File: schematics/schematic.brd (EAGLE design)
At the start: 134.6 x 64.8 mm, 25 parts, among them U1 TSR_1-2450

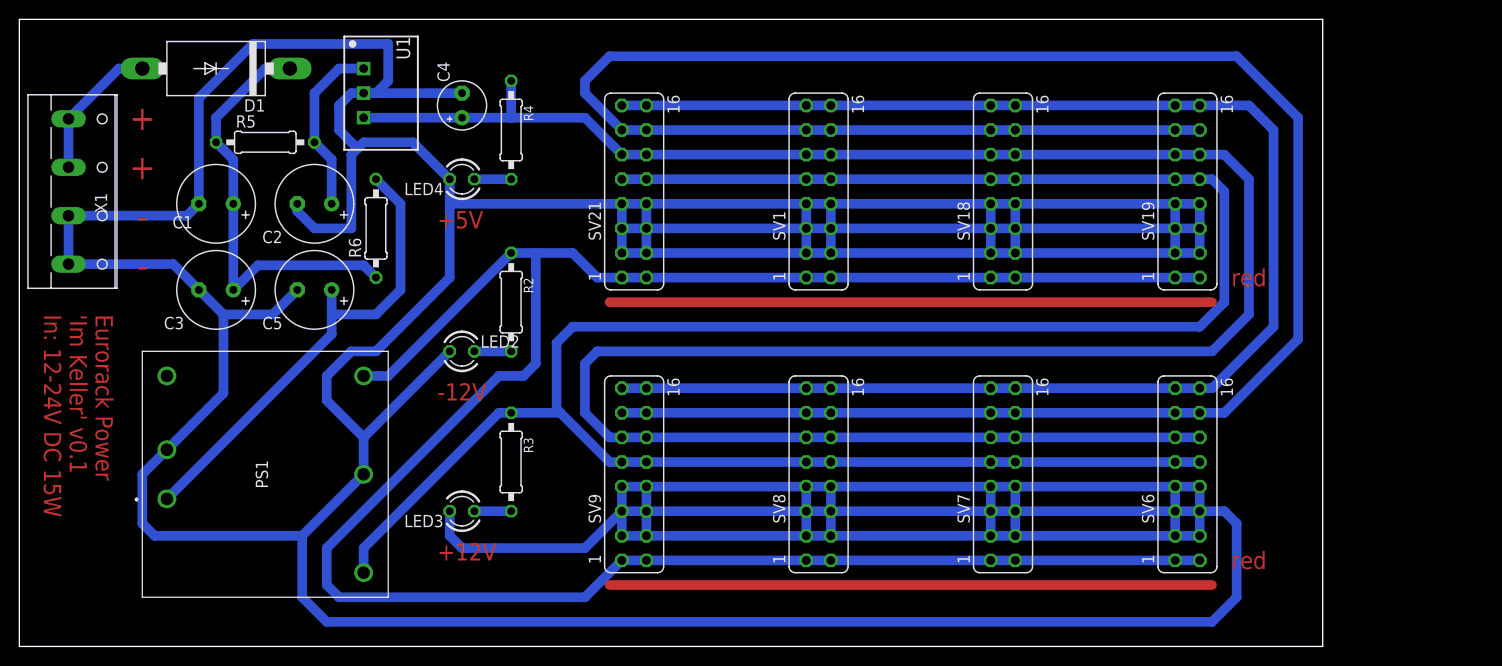
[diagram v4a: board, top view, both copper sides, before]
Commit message: changed distance of power headers
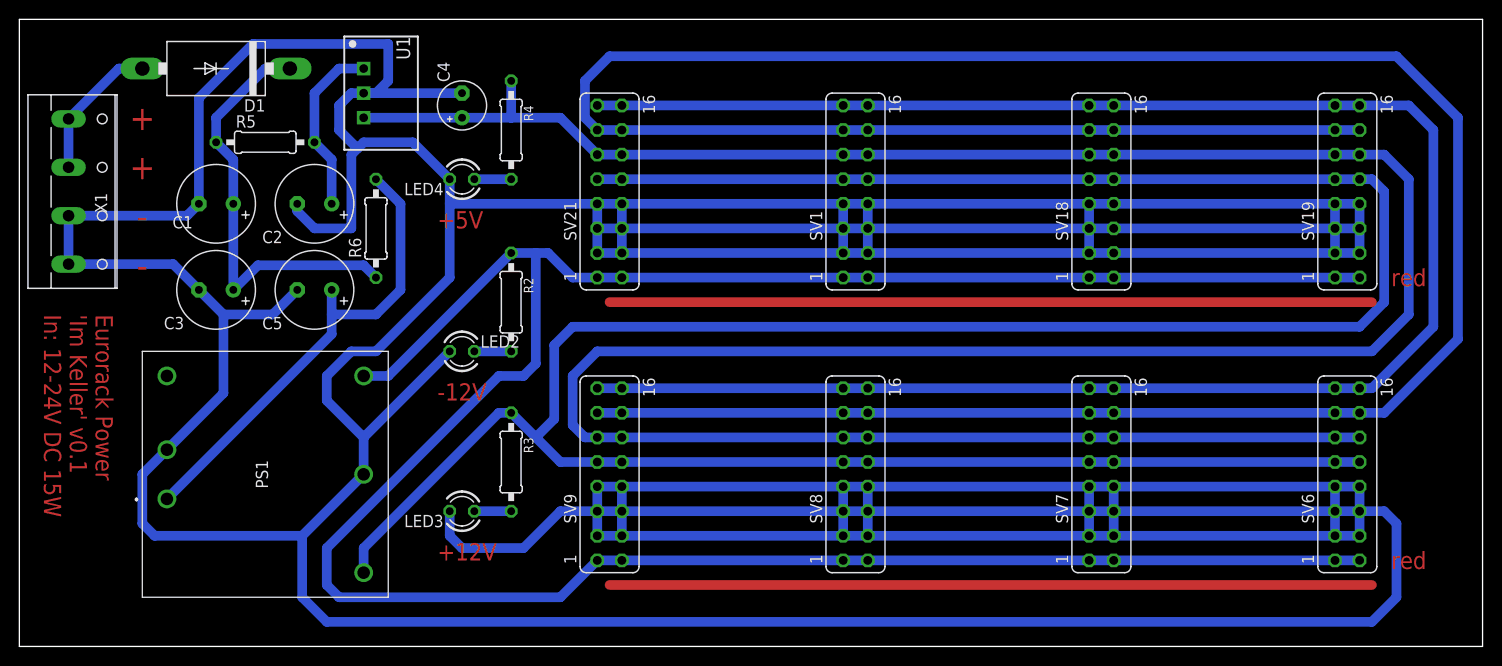
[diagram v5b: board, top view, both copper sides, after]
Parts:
- moved SV19 16.5 mm to (179.1, 45.7)
- moved SV6 16.5 mm to (179.1, 16.5)
- moved SV18 10.2 mm to (153.7, 45.7)
- moved SV7 10.2 mm to (153.7, 16.5)
- moved SV1 3.81 mm to (128.3, 45.7)
- moved SV8 3.81 mm to (128.3, 16.5)
- moved SV21 2.54 mm to (102.9, 45.7)
- moved SV9 2.54 mm to (102.9, 16.5)
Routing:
- net GND: track 829.9 -> 950.6 mm
- net +12V: track 249.1 -> 304.4 mm
- net CV: track 239.6 -> 293.1 mm
- net +5V: track 252.2 -> 304.2 mm
- net GATE: track 158.6 -> 196.7 mm
- net -12V: track 229.7 -> 262.7 mm
- net N$6: track 62.2 -> 78.7 mm
- net N$1: track 62.2 -> 78.7 mm
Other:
- board size 134.6 x 64.8 mm -> 151.1 x 64.8 mm

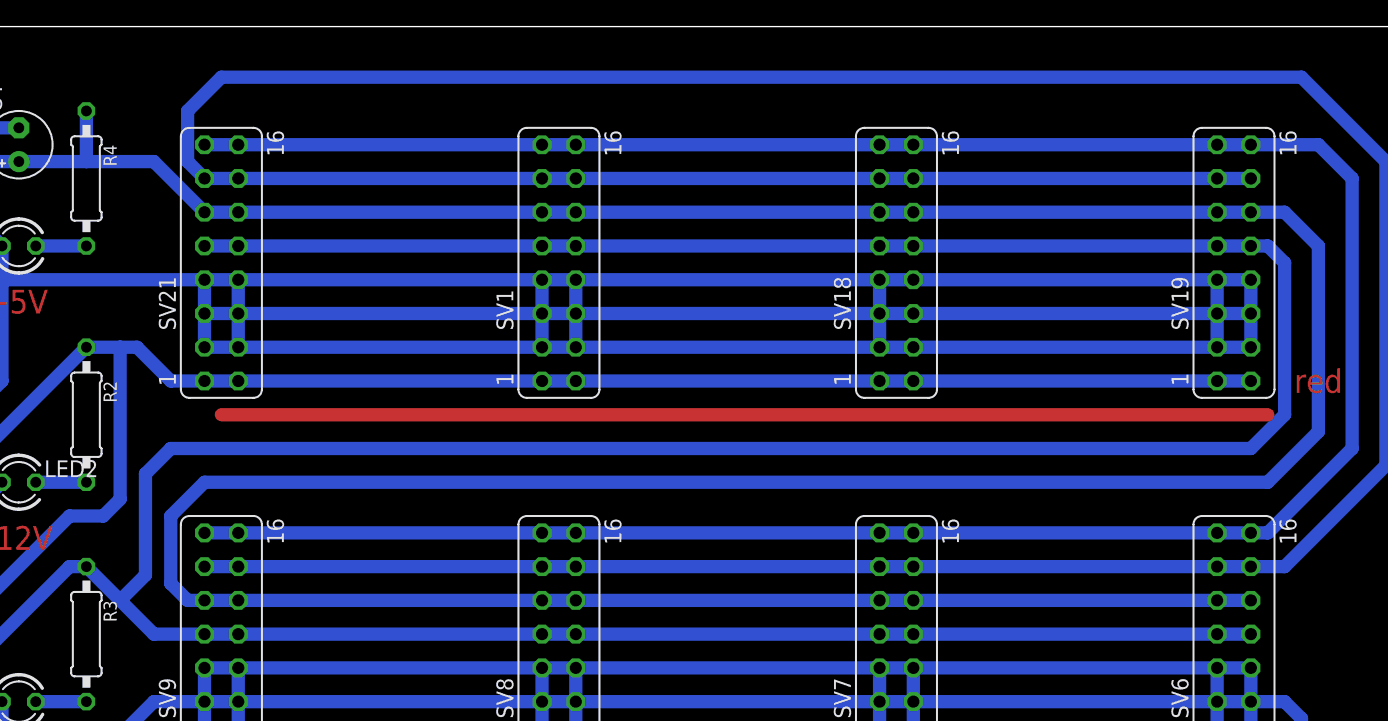
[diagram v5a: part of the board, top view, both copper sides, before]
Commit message: fixed wire clearance
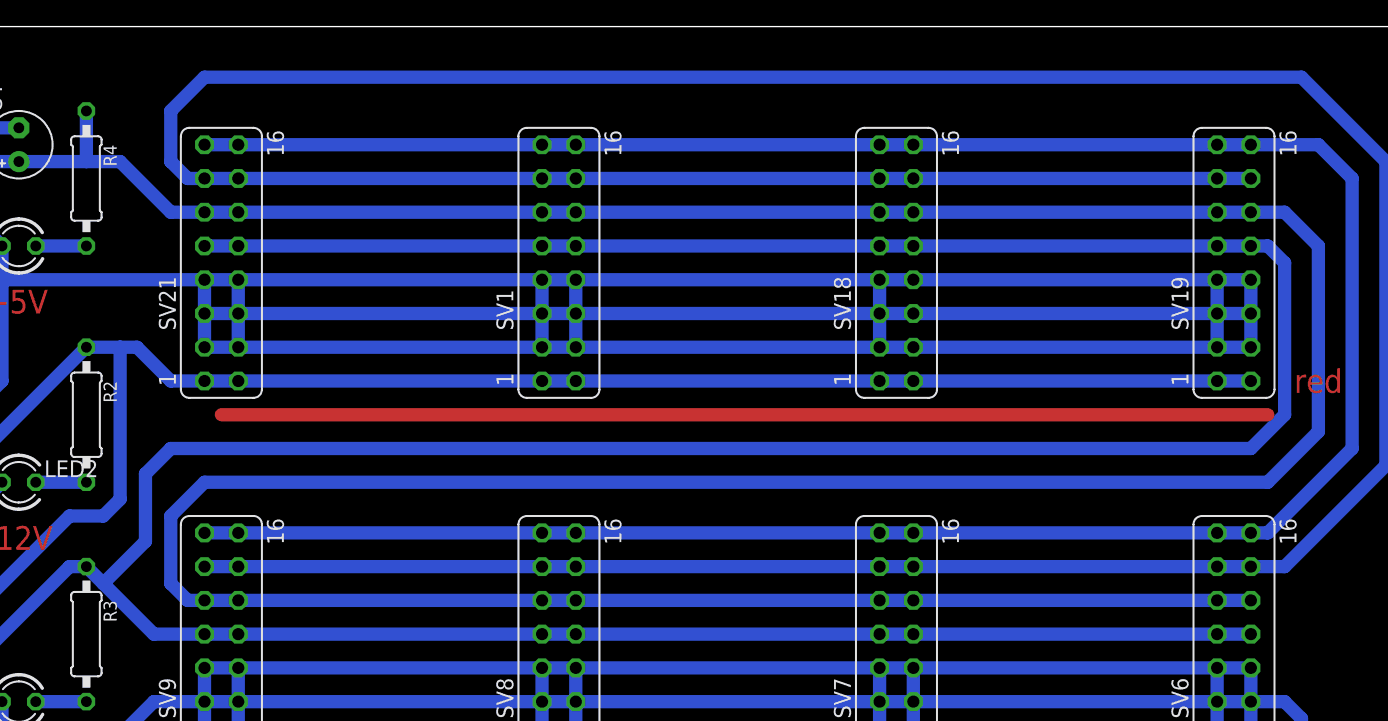
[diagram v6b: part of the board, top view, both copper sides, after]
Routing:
- net CV: track 293.1 -> 295.7 mm
- net +12V: track 304.4 -> 303.7 mm
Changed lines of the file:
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@@
 </class>
 </classes>
-<designrules name="default">
+<designrules name="default *">
 <description language="de">&lt;b&gt;EAGLE Design Rules&lt;/b&gt;
 &lt;p&gt;
@@
 <param name="mtCopper" value="0.035mm 0.035mm 0.035mm 0.035mm 0.035mm 0.035mm 0.035mm 0.035mm 0.035mm 0.035mm 0.035mm 0.035mm 0.035mm 0.035mm 0.035mm 0.035mm"/>
 <param name="mtIsolate" value="1.5mm 0.15mm 0.2mm 0.15mm 0.2mm 0.15mm 0.2mm 0.15mm 0.2mm 0.15mm 0.2mm 0.15mm 0.2mm 0.15mm 0.2mm"/>
-<param name="mdWireWire" value="6mil"/>
-<param name="mdWirePad" value="6mil"/>
-<param name="mdWireVia" value="6mil"/>
+<param name="mdWireWire" value="0.5mm"/>
+<param name="mdWirePad" value="0.5mm"/>
+<param name="mdWireVia" value="0.5mm"/>
 <param name="mdPadPad" value="6mil"/>
 <param name="mdPadVia" value="6mil"/>
@@
 <param name="mdDrill" value="6mil"/>
 <param name="mdSmdStop" value="0mil"/>
-<param name="msWidth" value="6mil"/>
+<param name="msWidth" value="0.8mm"/>
 <param name="msDrill" value="0.35mm"/>
 <param name="msMicroVia" value="9.99mm"/>
@@
 <wire x1="190.5" y1="53.34" x2="184.15" y2="59.69" width="1" layer="16"/>
 <wire x1="182.88" y1="22.86" x2="190.5" y2="30.48" width="1" layer="16"/>
-<wire x1="101.6" y1="52.07" x2="100.33" y2="53.34" width="1" layer="16"/>
-<wire x1="100.33" y1="53.34" x2="100.33" y2="57.15" width="1" layer="16"/>
-<wire x1="100.33" y1="57.15" x2="102.87" y2="59.69" width="1" layer="16"/>
-<wire x1="102.87" y1="59.69" x2="184.15" y2="59.69" width="1" layer="16"/>
+<wire x1="101.6" y1="52.07" x2="100.33" y2="52.07" width="1" layer="16"/>
+<wire x1="100.33" y1="52.07" x2="99.06" y2="53.34" width="1" layer="16"/>
+<wire x1="99.06" y1="53.34" x2="99.06" y2="57.15" width="1" layer="16"/>
+<wire x1="99.06" y1="57.15" x2="101.6" y2="59.69" width="1" layer="16"/>
+<wire x1="101.6" y1="59.69" x2="184.15" y2="59.69" width="1" layer="16"/>
 <wire x1="180.34" y1="52.07" x2="177.8" y2="52.07" width="1" layer="16"/>
 <wire x1="177.8" y1="52.07" x2="154.94" y2="52.07" width="1" layer="16"/>
@@
 <wire x1="77.47" y1="8.89" x2="91.44" y2="22.86" width="1" layer="16"/>
 <wire x1="99.06" y1="31.75" x2="97.155" y2="29.845" width="1" layer="16"/>
-<wire x1="92.71" y1="22.86" x2="95.25" y2="20.32" width="1" layer="16"/>
-<wire x1="95.25" y1="20.32" x2="97.79" y2="17.78" width="1" layer="16"/>
+<wire x1="92.71" y1="22.86" x2="93.98" y2="21.59" width="1" layer="16"/>
+<wire x1="93.98" y1="21.59" x2="97.79" y2="17.78" width="1" layer="16"/>
 <wire x1="97.79" y1="17.78" x2="101.6" y2="17.78" width="1" layer="16"/>
-<wire x1="97.155" y1="22.225" x2="95.25" y2="20.32" width="1" layer="16"/>
-<wire x1="97.155" y1="29.845" x2="97.155" y2="22.225" width="1" layer="16"/>
+<wire x1="97.155" y1="24.765" x2="93.98" y2="21.59" width="1" layer="16"/>
+<wire x1="97.155" y1="29.845" x2="97.155" y2="24.765" width="1" layer="16"/>
 </signal>
 <signal name="-12V">
@@
 <wire x1="77.47" y1="53.34" x2="87.63" y2="53.34" width="1" layer="16"/>
 <wire x1="87.63" y1="53.34" x2="92.71" y2="53.34" width="1" layer="16"/>
-<wire x1="92.71" y1="53.34" x2="97.79" y2="53.34" width="1" layer="16"/>
-<wire x1="97.79" y1="53.34" x2="101.6" y2="49.53" width="1" layer="16"/>
+<wire x1="92.71" y1="53.34" x2="95.25" y2="53.34" width="1" layer="16"/>
+<wire x1="99.06" y1="49.53" x2="95.25" y2="53.34" width="1" layer="16"/>
+<wire x1="99.06" y1="49.53" x2="101.6" y2="49.53" width="1" layer="16"/>
 <wire x1="92.71" y1="57.15" x2="92.71" y2="53.34" width="1" layer="16"/>
 <wire x1="180.34" y1="49.53" x2="182.88" y2="49.53" width="1" layer="16"/>

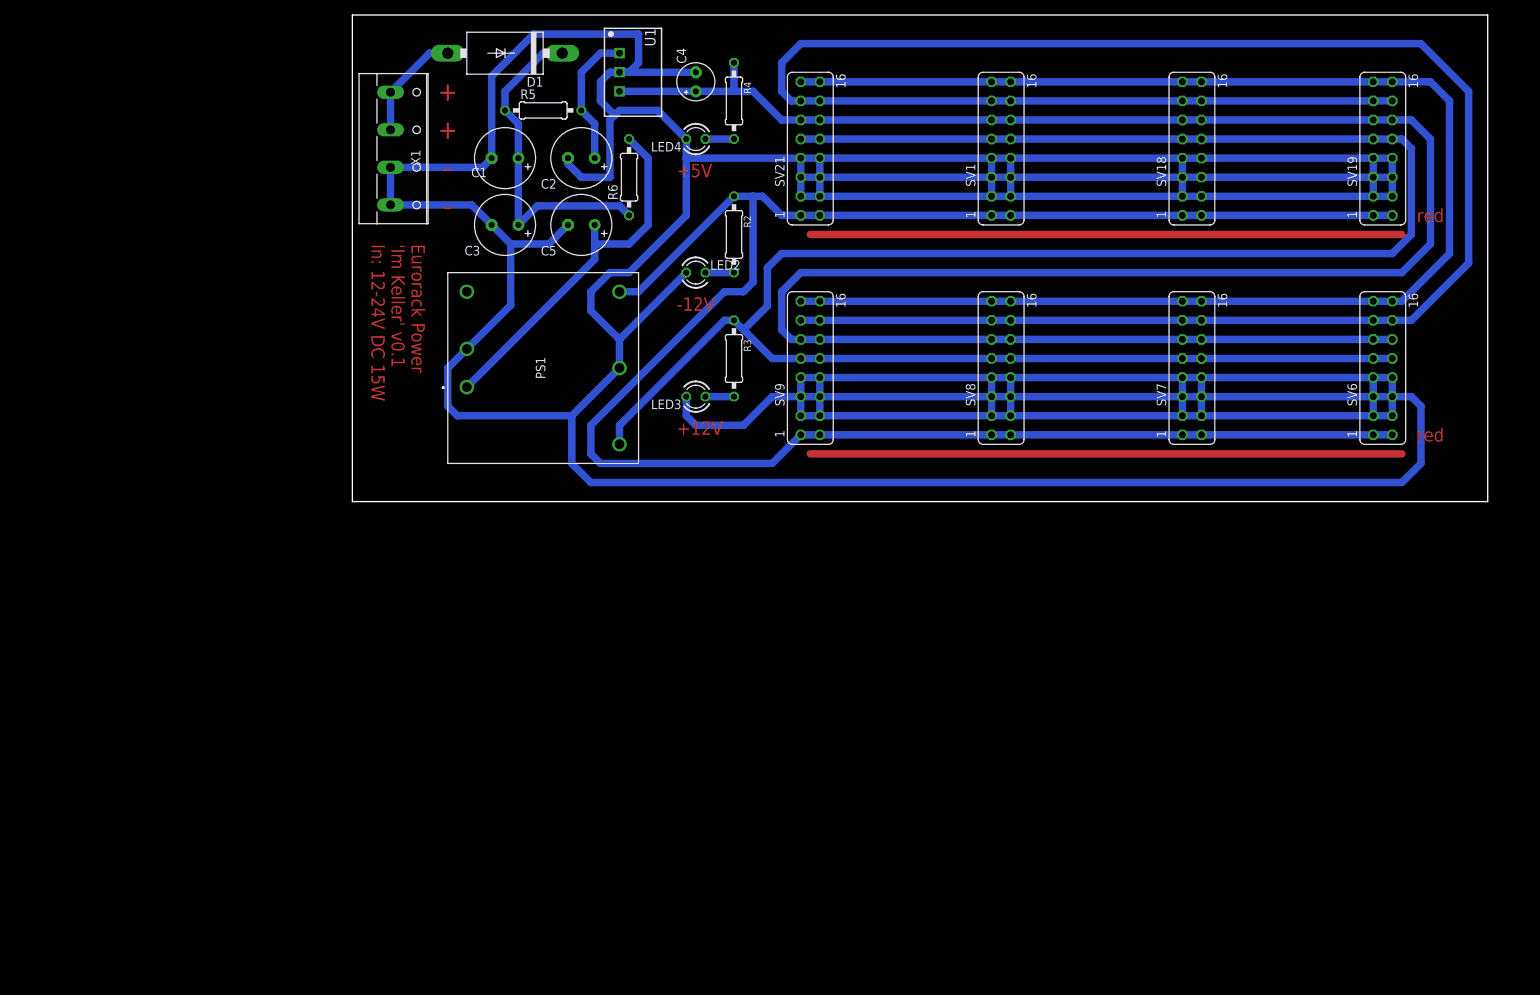
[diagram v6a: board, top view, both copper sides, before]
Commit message: added 4 more headers to board
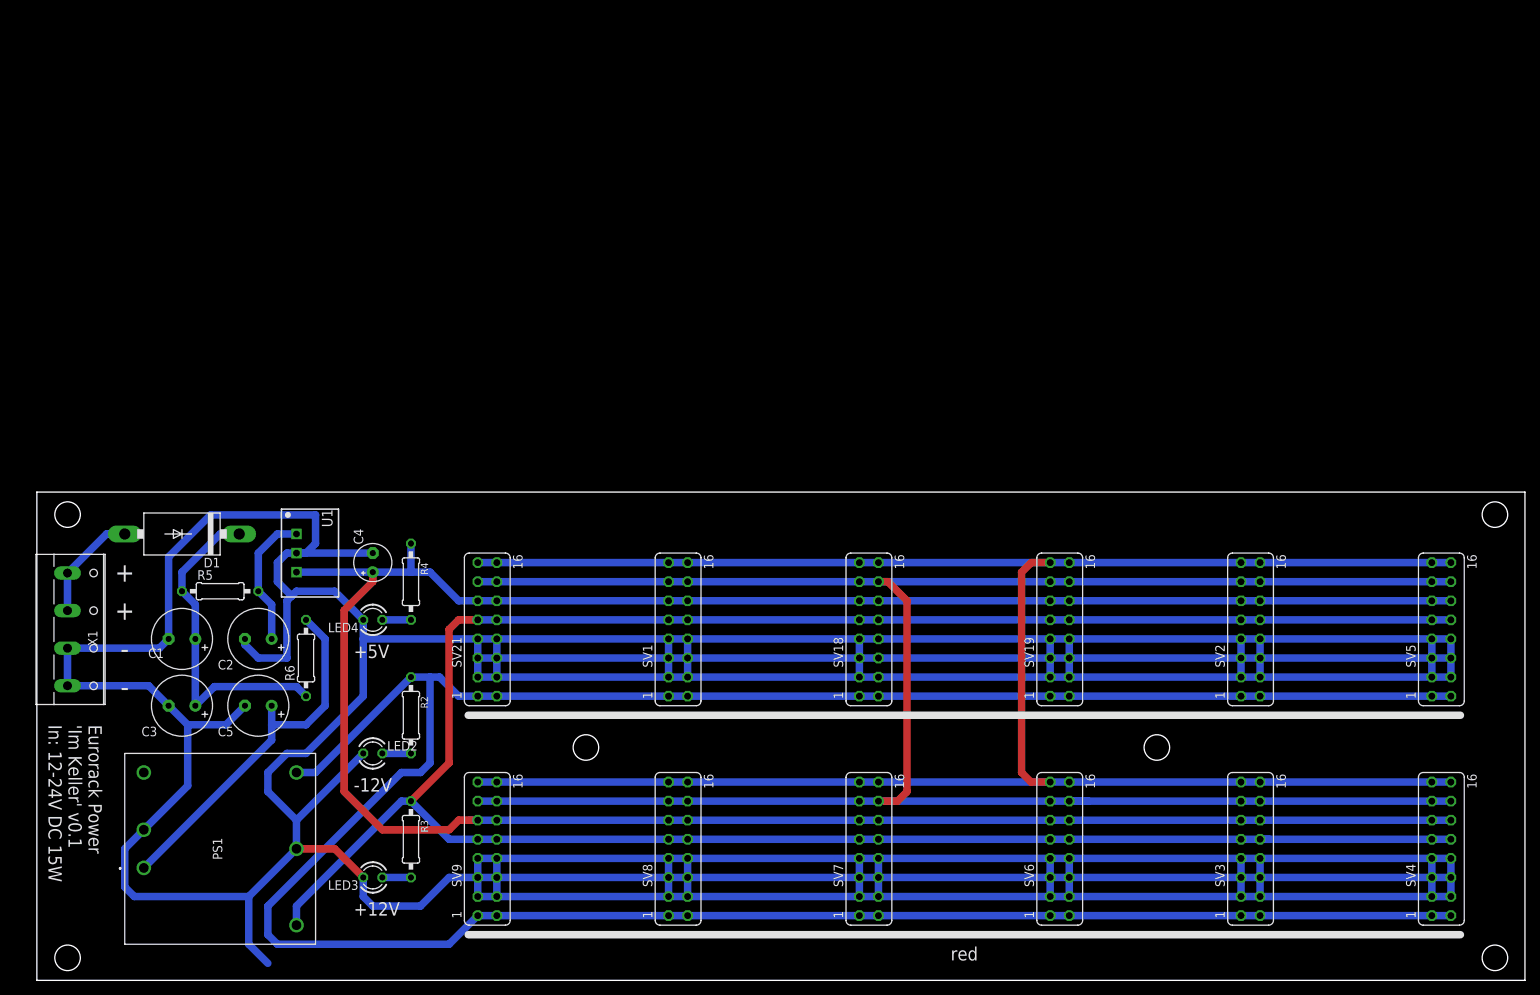
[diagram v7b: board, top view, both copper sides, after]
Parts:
- added SV2, SV3, SV4, SV5: (no value), con-lsta:FE08-2
- moved SV1 77.1 mm to (85.3, -18.3)
- moved SV21 77.1 mm to (59.9, -18.3)
- moved SV8 77.1 mm to (85.3, -47.5)
- moved SV9 77.1 mm to (59.9, -47.5)
- moved C1 77.1 mm to (19.2, -19.6)
- moved C2 77.1 mm to (29.4, -19.6)
- moved C3 77.1 mm to (19.2, -28.4)
- moved C4 77.1 mm to (44.6, -9.39)
- moved C5 77.1 mm to (29.4, -28.4)
- moved D1 77.1 mm to (19.2, -5.58)
- moved LED2 77.1 mm to (44.6, -34.8)
- moved LED3 77.1 mm to (44.6, -51.3)
- moved LED4 77.1 mm to (44.6, -17.0)
- moved PS1 77.1 mm to (14.2, -50.0)
- moved R2 77.1 mm to (49.7, -29.7)
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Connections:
- net +12V: now also SV2.10, SV2.9, SV3.10, SV3.9, SV4.10, SV4.9, SV5.10, SV5.9
- net +5V: now also SV2.11, SV2.12, SV3.11, SV3.12, SV4.11, SV4.12, SV5.11, SV5.12
- net -12V: now also SV2.1, SV2.2, SV3.1, SV3.2, SV4.1, SV4.2, SV5.1, SV5.2
- net CV: now also SV2.13, SV2.14, SV3.13, SV3.14, SV4.13, SV4.14, SV5.13, SV5.14
- net GATE: now also SV2.15, SV2.16, SV3.15, SV3.16, SV4.15, SV4.16, SV5.15, SV5.16
- net GND: now also SV2.3, SV2.4, SV2.5, SV2.6, SV2.7, SV2.8, SV3.3, SV3.4, SV3.5, SV3.6, SV3.7, SV3.8, SV4.3, SV4.4, SV4.5, SV4.6, SV4.7, SV4.8, SV5.3, SV5.4, SV5.5, SV5.6, SV5.7, SV5.8
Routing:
- net GND: track 950.6 -> 1183.0 mm
- net -12V: track 262.7 -> 364.3 mm
- net GATE: track 196.7 -> 294.4 mm
- net N$6: track 78.7 -> 0.00 mm
- net N$1: track 78.7 -> 0.00 mm
- net +5V: track 304.2 -> 341.1 mm
- net +12V: track 303.7 -> 324.2 mm
- net CV: track 295.7 -> 296.2 mm
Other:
- board size 151.1 x 64.8 mm -> 198.1 x 65 mm

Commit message: some minor fixes on schematic
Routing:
- net GND: track 1183.0 -> 1178.1 mm
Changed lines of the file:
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@@
 <text x="11.61" y="-20.82" size="2.54" layer="21" align="center">-</text>
 <text x="11.61" y="-25.9" size="2.54" layer="21" align="center">-</text>
-<text x="123.37" y="-32.25" size="1.778" layer="22" rot="MR0" align="center">red</text>
+<text x="123.37" y="-32.25" size="1.778" layer="21" align="center">red</text>
 <text x="123.37" y="-61.46" size="1.778" layer="21" align="center">red</text>
 <dimension x1="59.87" y1="-8.12" x2="85.27" y2="-8.12" x3="72.57" y3="-6.85" textsize="1.778" layer="47"/>
@@
 <dimension x1="136.07" y1="-8.12" x2="161.47" y2="-8.12" x3="148.77" y3="-6.85" textsize="1.778" layer="47"/>
 <dimension x1="161.47" y1="-8.12" x2="186.87" y2="-8.12" x3="174.17" y3="-6.85" textsize="1.778" layer="47"/>
-<dimension x1="0" y1="0" x2="0" y2="-65" x3="-4" y3="-32.5" textsize="1.778" layer="20"/>
-<dimension x1="0" y1="-65" x2="198" y2="-65" x3="99" y3="-69" textsize="1.778" layer="20"/>
+<dimension x1="0" y1="0" x2="0" y2="-65" x3="-4" y3="-32.5" textsize="1.778" layer="47"/>
+<dimension x1="0" y1="-65" x2="198" y2="-65" x3="99" y3="-69" textsize="1.778" layer="47"/>
 <hole x="4" y="-3" drill="3.4"/>
 <hole x="4" y="-62" drill="3.4"/>
@@
 <wire x1="27.612" y1="-20.312" x2="27.612" y2="-19.55" width="1" layer="16"/>
 <wire x1="31.93" y1="-9.39" x2="31.93" y2="-11.93" width="1" layer="16"/>
-<wire x1="28.12" y1="-53.84" x2="28.12" y2="-60.19" width="1" layer="16"/>
-<wire x1="28.12" y1="-60.19" x2="30.66" y2="-62.73" width="1" layer="16"/>
 <wire x1="34.47" y1="-47.49" x2="34.47" y2="-43.68" width="1" layer="16"/>
 <wire x1="30.66" y1="-39.87" x2="34.47" y2="-43.68" width="1" layer="16"/>
@@
 <wire x1="185.6" y1="-51.3" x2="188.14" y2="-51.3" width="1" layer="16"/>
 <wire x1="185.6" y1="-53.84" x2="185.6" y2="-48.76" width="1" layer="16"/>
+<wire x1="111.94" y1="-19.55" x2="111.94" y2="-24.63" width="1" layer="16"/>
 </signal>
 <signal name="+15V">
